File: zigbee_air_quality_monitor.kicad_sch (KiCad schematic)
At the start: 30 parts, among them J1 USB_C_Receptacle_USB2.0, J2 QWIIC, J3 Conn_02x02_Odd_Even, SW1 PAIR_BTN, SW2 USER_BTN, U1 USBLC6-2SC6, U2 BT840, U3 XC6206P332MR, U4 SCD40-D-R2, U6 TXS0102DCU

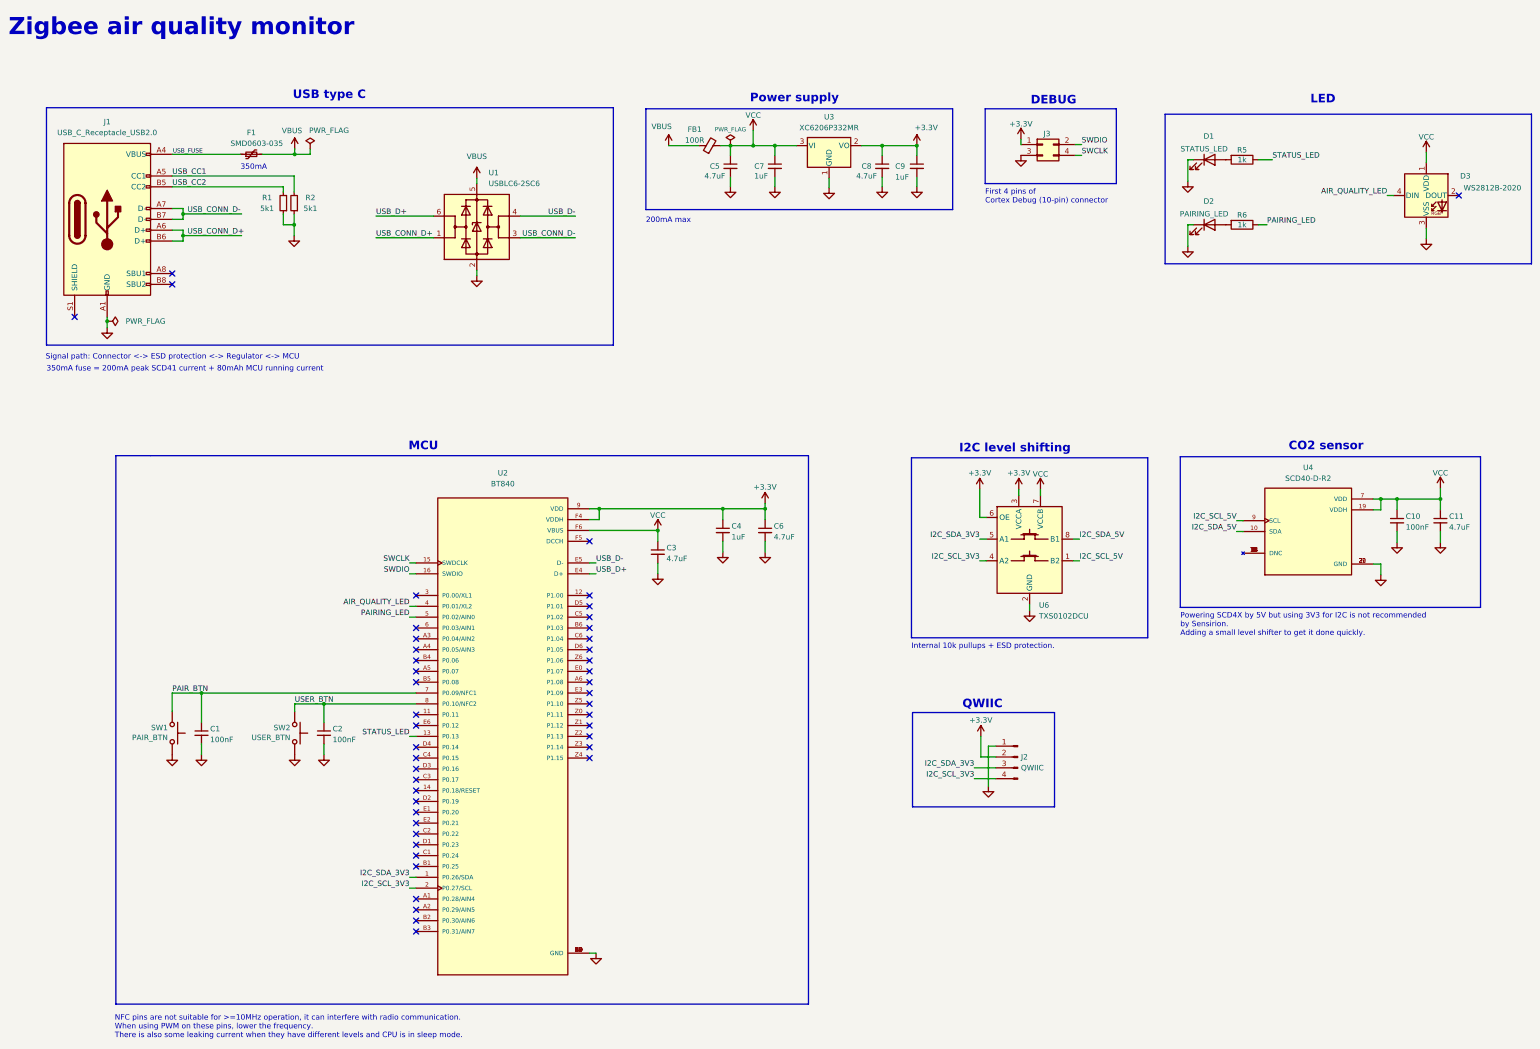
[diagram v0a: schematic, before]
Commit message: Cost optimizations
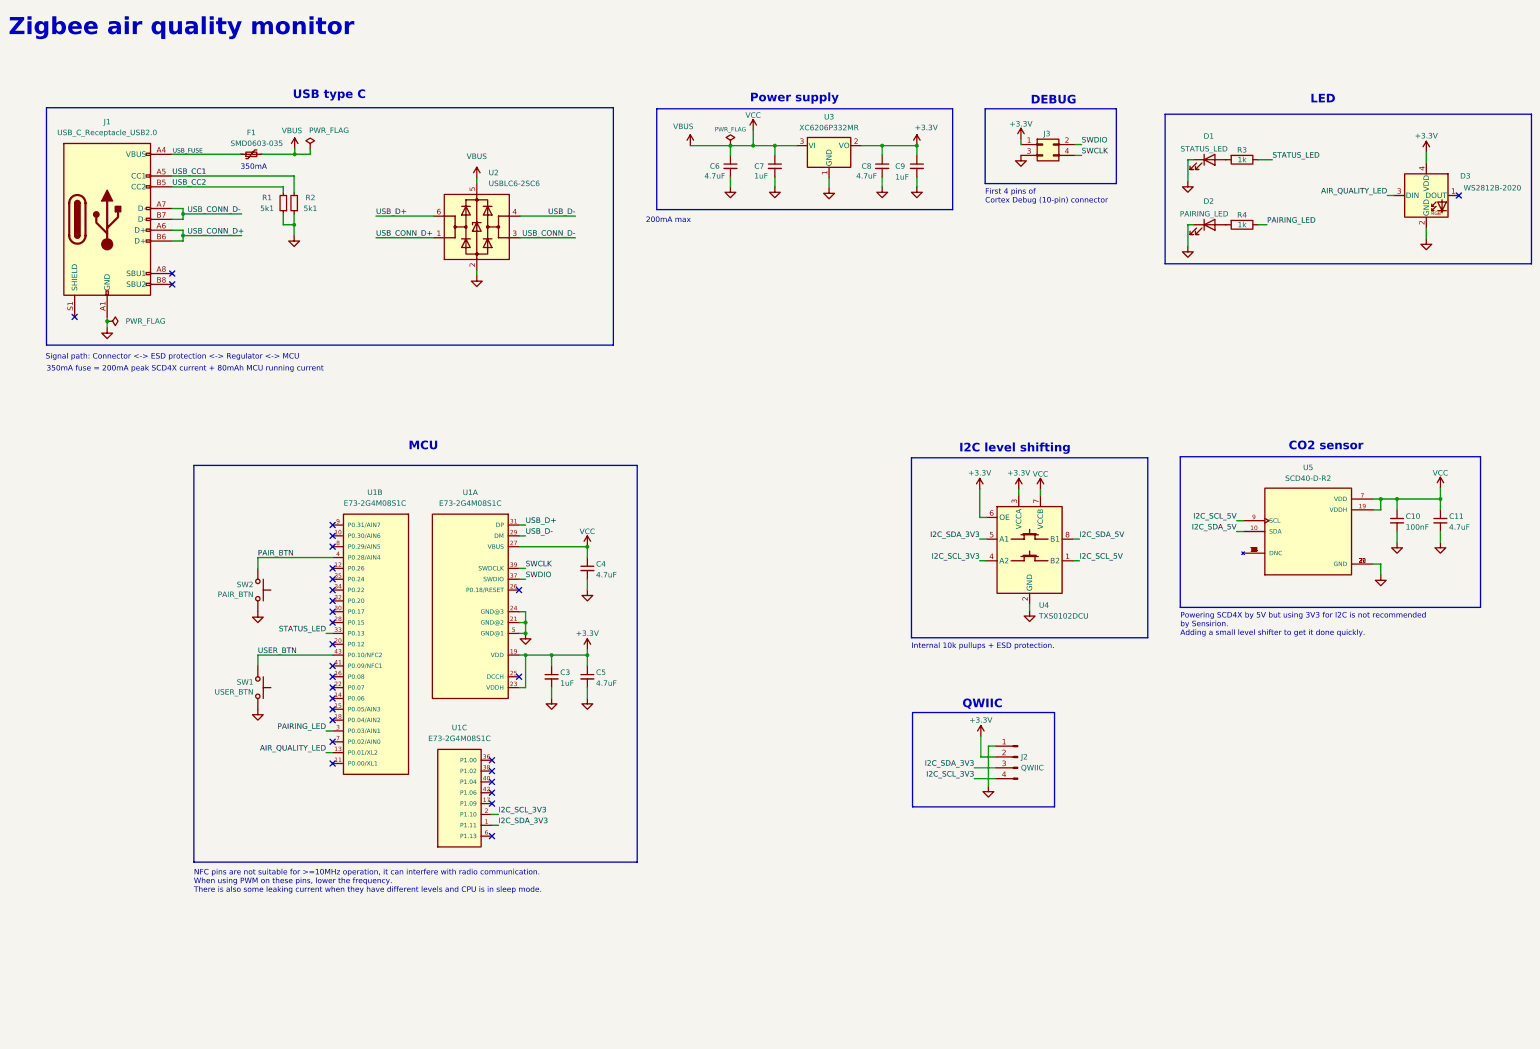
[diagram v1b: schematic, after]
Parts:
- removed C1, C2: 100nF, Capacitor_SMD:C_0603_1608Metric, symbol Device:C_Small
- removed FB1: 100R, Inductor_SMD:L_0603_1608Metric, symbol Device:FerriteBead_Small
- removed U2: BT840, zigbee_air_quality_monitor:BT840, symbol hangy:BT840
- added U1: E73-2G4M08S1C, zigbee_air_quality_monitor:E73-2G4M08S1C, symbol zigbee_air_quality_monitor:E73-2G4M08S1C
- C10: LCSC Part (none) -> C14663
- C11: LCSC Part (none) -> C19666
- C3: renamed from C4; LCSC Part (none) -> C15849
- C4: renamed from C3; LCSC Part (none) -> C19666
- C5: renamed from C6; LCSC Part (none) -> C19666
- C6: renamed from C5; LCSC Part C1705 -> C19666
- C7, C9: LCSC Part C1592 -> C15849
- C8: LCSC Part C1705 -> C19666
- F1: LCSC Part (none) -> C910818
- R1, R2: LCSC Part C105580 -> C23186
- R3: renamed from R5; LCSC Part (none) -> C21190
- R4: renamed from R6; LCSC Part (none) -> C21190
- U4: renamed from U6; LCSC Part (none) -> C53434
- U5: renamed from U4; footprint zigbee_air_quality_monitor:XDCR_SCD41-D-R2 -> zigbee_air_quality_monitor:XDCR_SCD40-D-R2; LCSC Part (none) -> C3659421
- renumbered SW2 to SW1, SW1 to SW2, U1 to U2
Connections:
- net +3.3V: now also D3.4 (VDD), U1.19 (VDD), U1.23 (VDDH)
- net AIR_QUALITY_LED: now also D3.3 (DIN), U1.13 (P0.01/XL2); no longer D3.4 (DIN)
- net GND: now also D3.2 (GND), U1.21 (GND@2), U1.24 (GND@3), U1.5 (GND@1); no longer D3.3 (VSS)
- net I2C_SCL_3V3: now also U1.2 (P1.10)
- net I2C_SDA_3V3: now also U1.1 (P1.11)
- net PAIRING_LED: now also U1.3 (P0.03/AIN1)
- net PAIR_BTN: now also U1.4 (P0.28/AIN4)
- net STATUS_LED: now also U1.33 (P0.13)
- net SWCLK: now also U1.39 (SWDCLK)
- net SWDIO: now also U1.37 (SWDIO)
- net USB_D+: now also U1.31 (DP)
- net USB_D-: now also U1.29 (DM)
- net USER_BTN: now also U1.43 (P0.10/NFC2)
- net VBUS: now also C10.1, C11.1, C4.1, C6.1, C7.1, U3.3 (VI), U4.7 (VCCB), U5.19 (VDDH), U5.7 (VDD), U1.27 (VBUS)
- removed net VCC: C10.1, C11.1, C4.1, C6.1, C7.1, D3.1 (VDD), U3.3 (VI), U4.7 (VCCB), U5.19 (VDDH), U5.7 (VDD)
- no-connect marks 46 -> 30
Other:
- note added: "350mA fuse = 200mA peak SCD4X current + 80mAh MCU running current"
- note removed: "350mA fuse = 200mA peak SCD41 current + 80mAh MCU running current"
- moved on the sheet: C3, C4, C5, SW1, SW2
